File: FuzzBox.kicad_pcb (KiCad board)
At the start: 2 copper layers, 152.4 x 58.4 mm, 20 parts, among them J1 AudioJack2, J2 AudioJack2, SW1 SW_SPST, U1 LM741CN/NOPB, U2 LM741CN/NOPB

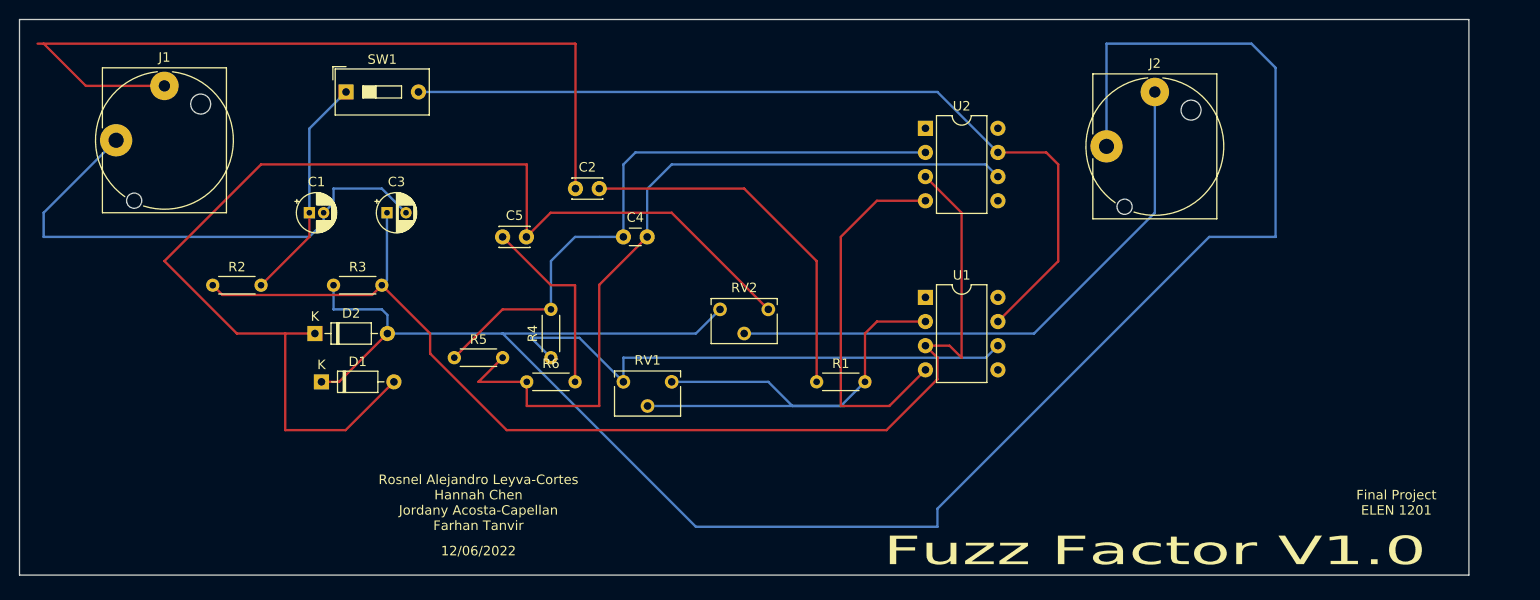
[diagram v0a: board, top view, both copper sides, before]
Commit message: updated schem + PCB
changed the layout to reflect an increased gain for fabrication
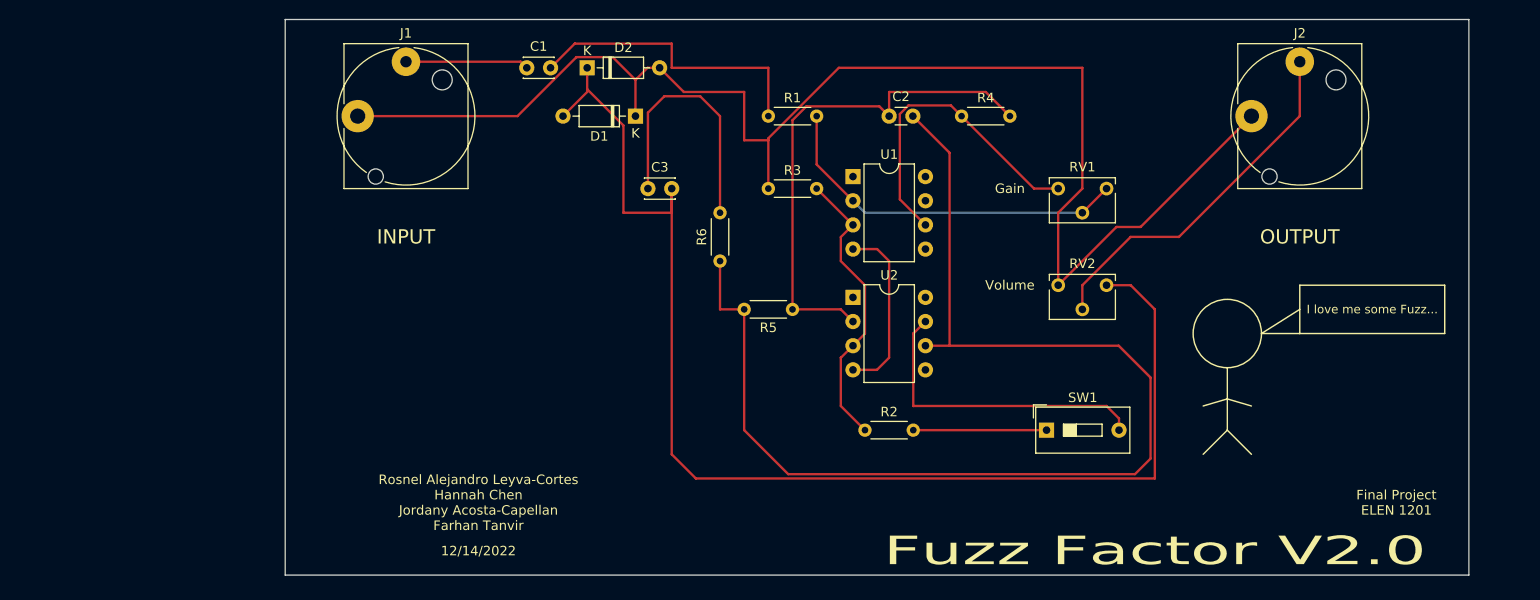
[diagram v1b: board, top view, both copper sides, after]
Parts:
- removed C4: 22p, Capacitor_THT:C_Disc_D3.0mm_W1.6mm_P2.50mm
- removed C5: .22u, Capacitor_THT:C_Disc_D3.0mm_W2.0mm_P2.50mm
- C1: value 100u -> 0.22u; footprint Capacitor_THT:CP_Radial_D4.0mm_P1.50mm -> Capacitor_THT:C_Disc_D3.0mm_W2.0mm_P2.50mm
- C2: value 22u -> .22p; footprint Capacitor_THT:C_Disc_D3.0mm_W2.0mm_P2.50mm -> Capacitor_THT:C_Disc_D3.0mm_W1.6mm_P2.50mm
- C3: value 10u -> .22u; footprint Capacitor_THT:CP_Radial_D4.0mm_P2.00mm -> Capacitor_THT:C_Disc_D3.0mm_W2.0mm_P2.50mm
- R1: value 47k -> 500
- R4: value 4.7k -> 2k
- R5: value 33k -> 60k
- RV1: value 500k -> 500K
- moved SW1 81.8 mm to (179.1, 116.8)
- moved R2 70.3 mm to (160.0, 116.8)
- moved R4 50.1 mm to (170.2, 83.8), turned to 0 degrees
- moved RV1 50.0 mm to (185.4, 91.4)
- moved R3 46.8 mm to (149.9, 91.4)
- moved D1 43.3 mm to (135.9, 83.8), turned to 180 degrees
- moved D2 40.0 mm to (130.8, 78.7)
- moved R5 35.9 mm to (152.4, 104.1), turned to 180 degrees
- moved RV2 35.7 mm to (185.4, 101.6)
- moved C2 33.8 mm to (162.6, 83.8)
- moved R1 28.4 mm to (149.9, 83.8)
- moved C3 27.6 mm to (137.2, 91.4)
- moved C1 27.5 mm to (124.5, 78.7)
- moved J1 25.5 mm to (111.8, 78.1)
- moved R6 24.0 mm to (144.8, 99.1), turned to 90 degrees
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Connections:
- C1 pad 2: GND -> Net-(C1-Pad2)
- C3 pad 2: GND -> Net-(C3-Pad2)
- D1 pad 2: Net-(C5-Pad2) -> Net-(C3-Pad2)
- D2 pad 1: Net-(C5-Pad2) -> Net-(C3-Pad2)
- J1 pad T: Net-(C2-Pad1) -> Net-(C1-Pad1)
- R1 pad 1: Net-(C2-Pad2) -> Net-(C1-Pad2)
- R2 pad 1: Net-(C3-Pad1) -> Net-(R2-Pad1)
- R2 pad 2: Net-(C1-Pad1) -> Net-(R2-Pad2)
- R3 pad 2: Net-(C3-Pad1) -> Net-(R2-Pad1)
- R4 pad 2: Net-(C4-Pad1) -> Net-(C2-Pad1)
- R5 pad 1: Net-(C4-Pad1) -> Net-(C2-Pad1)
- R5 pad 2: Net-(C4-Pad2) -> Net-(C2-Pad2)
- R6 pad 1: Net-(C4-Pad2) -> Net-(C2-Pad2)
- R6 pad 2: Net-(C5-Pad1) -> Net-(C3-Pad1)
- RV2 pad 1: Net-(C5-Pad2) -> Net-(C3-Pad2)
- SW1 pad 1: Net-(C1-Pad1) -> Net-(R2-Pad2)
- U1 pad 3: Net-(C3-Pad1) -> Net-(R2-Pad1)
- U2 pad 2: Net-(C4-Pad1) -> Net-(C2-Pad1)
- U2 pad 3: Net-(C3-Pad1) -> Net-(R2-Pad1)
- U2 pad 6: Net-(C4-Pad2) -> Net-(C2-Pad2)
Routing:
- net Net-(C3-Pad2): track 0.00 -> 132.0 mm
- net Net-(C5-Pad2): track 123.3 -> 0.00 mm
- net GND: track 262.4 -> 150.2 mm
- net Net-(C3-Pad1): track 123.6 -> 27.3 mm
- net Net-(C2-Pad2): track 38.7 -> 125.0 mm
- net Net-(C4-Pad2): track 82.2 -> 0.00 mm
- net Net-(C4-Pad1): track 65.9 -> 0.00 mm
- net +9V: track 89.6 -> 32.8 mm
- net Net-(C2-Pad1): track 86.3 -> 54.3 mm
- net Net-(C1-Pad2): track 0.00 -> 31.6 mm
- net Net-(R2-Pad1): track 0.00 -> 30.7 mm
- net Net-(R4-Pad1): track 57.0 -> 33.4 mm
- net Net-(J2-PadT): track 61.1 -> 38.5 mm
- net -9V: track 38.7 -> 18.8 mm
- net Net-(C5-Pad1): track 19.9 -> 0.00 mm
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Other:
- board size 152.4 x 58.4 mm -> 124.5 x 58.4 mm
- board text added: "12/14/2022"
- board text added: "Columbia University ELEN 1201 Final Project"
- board text added: "Fuzz Factor V2.0"
- board text added: "Gain"
- board text added: "INPUT"
- board text added: "OUTPUT"
- board text added: "Volume"
- board text added: "dim: 124.46mm x 58.42mm"
- board text removed: "12/06/2022"
- board text removed: "Fuzz Factor V1.0"
- board text removed: "FuzzBoxSchematic"
- board text removed: "dim: 152.4mm x 58.42mm"
